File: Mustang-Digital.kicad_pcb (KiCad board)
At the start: 4 copper layers, 67 x 105.4 mm, 125 parts, among them IC307 TPD4E1B06DRLR, IC308 TPD4E1B06DRLR, J1 685119248123_Left, J2 685119248123_Left, J3 Conn_01x02_Pin_JST-PH_Batt, J303 2130830005, J4 Micro_SD_Card_4.0_CUI, U1 BM83SM1-00TB, U2 LP5012RUKR, U3 STM32L496VGTx, U301 SPU03L-05, U302 SPU03L-05, U303 SPU03L-05, U304 ADUM4160BRWZ, U305 USB2422T-I/MJ, U306 BQ24296RGER, U307 TPD4E1B06DRLR, U308 TPD4E1B06DRLR

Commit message: wip
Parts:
- added C12: 1uF, Mustang_Library:C_0805_2012Metric_Pad1.18x1.45mm_HandSolder, F.Cu at (133.5, 113.0)
- added C13: 1uF, Mustang_Library:C_0805_2012Metric_Pad1.18x1.45mm_HandSolder, F.Cu at (136.5, 113.0)
- added U4: LP5907MFX-3.3_NOPB, Mustang_Library:SOT95P280X145-5N, F.Cu at (135.0, 116.8)
- J1, J2: value 685119248123_Left -> 685119248123
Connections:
- net /Buds/IMU_CSR renamed /Buds/HR_INTR
- net /Buds/SPK_AUDIO+L renamed /BT/SPK_AUDIO+L
- net /Buds/SPK_AUDIO+R renamed /BT/SPK_AUDIO+R
- net /Buds/SPK_AUDIO-L renamed /BT/SPK_AUDIO-L
- net /Buds/SPK_AUDIO-R renamed /BT/SPK_AUDIO-R
- net /Buds/TALK_MICL renamed /BT/TALK_MICL
- net /Buds/TALK_MICR renamed /BT/TALK_MICR
- net /Charging_Isolation/5V renamed /Charging_USB/5V
- net /Charging_Isolation/BAT renamed /Charging_USB/BAT
- net /Charging_Isolation/BTST renamed /Charging_USB/BTST
- net /Charging_Isolation/CRFILT renamed /Charging_USB/CRFILT
- net /Charging_Isolation/DM1 renamed /Charging_USB/DM1
- net /Charging_Isolation/DM2 renamed /Charging_USB/DM2
- net /Charging_Isolation/DP1 renamed /Charging_USB/DP1
- net /Charging_Isolation/DP2 renamed /Charging_USB/DP2
- net /Charging_Isolation/ILIM renamed /Charging_USB/ILIM
- net /Charging_Isolation/OCS1_N renamed /Charging_USB/OCS1_N
- net /Charging_Isolation/OCS2_N renamed /Charging_USB/OCS2_N
- net /Charging_Isolation/PLLFILT renamed /Charging_USB/PLLFILT
- net /Charging_Isolation/PMID renamed /Charging_USB/PMID
- net /Charging_Isolation/PRTPWR1 renamed /Charging_USB/PRTPWR1
- net /Charging_Isolation/PRTPWR2 renamed /Charging_USB/PRTPWR2
- net /Charging_Isolation/RBIAS renamed /Charging_USB/RBIAS
- net /Charging_Isolation/REGN renamed /Charging_USB/REGN
- net /Charging_Isolation/RESET_N renamed /Charging_USB/RESET_N
- net /Charging_Isolation/SW renamed /Charging_USB/SW
- net /Charging_Isolation/TS renamed /Charging_USB/TS
- net /Charging_Isolation/VBUS1 renamed /Charging_USB/VBUS1
- net /Charging_Isolation/VBUS_DET renamed /Charging_USB/VBUS_DET
- net /Charging_Isolation/VOUT1 renamed /Charging_USB/VOUT1
- net /Charging_Isolation/VOUT2 renamed /Charging_USB/VOUT2
- net /Charging_Isolation/VOUT3 renamed /Charging_USB/VOUT3
- net /Charging_Isolation/XIN renamed /Charging_USB/XIN
- net /Charging_Isolation/XOUT renamed /Charging_USB/XOUT
- net /LEDS_BUTTONS_SWITCHES/LED_EN renamed /LEDs_Switches/LED_EN
- net /LEDS_BUTTONS_SWITCHES/LED_SCL renamed /LEDs_Switches/LED_SCL
- net /LEDS_BUTTONS_SWITCHES/LED_SDA renamed /LEDs_Switches/LED_SDA
- net /LEDS_BUTTONS_SWITCHES/SW_BTPAIR renamed /LEDs_Switches/SW_BTPAIR
- net /LEDS_BUTTONS_SWITCHES/SW_PLAY renamed /LEDs_Switches/SW_PLAY
- net /LEDS_BUTTONS_SWITCHES/SW_PWR renamed /LEDs_Switches/SW_PWR
- net /LEDS_BUTTONS_SWITCHES/SW_RECORD renamed /LEDs_Switches/SW_RECORD
- C302 pad 2: /Charging_Isolation/VDD1 -> /Charging_USB/VDD1
- C306 pad 1: /Charging_Isolation/VSYS -> /Charging_USB/VSYS
- C307 pad 1: /Charging_Isolation/VSYS -> /Charging_USB/VSYS
- C315 pad 2: /Charging_Isolation/VBUS0 -> /Charging_USB/VBUS0
- C316 pad 2: /Charging_Isolation/VBUS0 -> /Charging_USB/VBUS0
- C7 pad 2: /Buds/VSYS -> /Charging_USB/VSYS
- C8 pad 2: /Buds/VSYS -> /Charging_USB/VSYS
- J1 pad 5: /Buds/VSYS -> /Charging_USB/VSYS
- J2 pad 5: /Buds/VSYS -> /Charging_USB/VSYS
- J303 pad A4: /Charging_Isolation/VBUS0 -> /Charging_USB/VBUS0
- J303 pad A5: /Charging_Isolation/CC1 -> /Charging_USB/CC1
- J303 pad A6: /Charging_Isolation/DA+ -> /Charging_USB/DAB+
- J303 pad A7: /Charging_Isolation/DB- -> /Charging_USB/DAB-
- J303 pad A8: /Charging_Isolation/SBU1 -> /Charging_USB/SBU1
- J303 pad A9: /Charging_Isolation/VBUS0 -> /Charging_USB/VBUS0
- J303 pad B4: /Charging_Isolation/VBUS0 -> /Charging_USB/VBUS0
- J303 pad B5: /Charging_Isolation/CC2 -> /Charging_USB/CC2
- J303 pad B6: /Charging_Isolation/DA+ -> /Charging_USB/DAB+
- J303 pad B7: /Charging_Isolation/DB- -> /Charging_USB/DAB-
- J303 pad B8: /Charging_Isolation/SBU2 -> /Charging_USB/SBU2
- J303 pad B9: /Charging_Isolation/VBUS0 -> /Charging_USB/VBUS0
- L301 pad 2: /Charging_Isolation/VSYS -> /Charging_USB/VSYS
- L305 pad 2: /Charging_Isolation/VBUS0 -> /Charging_USB/VBUS0
- L306 pad 2: /Charging_Isolation/VBUS0 -> /Charging_USB/VBUS0
- R312 pad 2: /Charging_Isolation/PG -> /Charging_USB/PG
- R313 pad 2: /Charging_Isolation/STAT -> /Charging_USB/STAT
- R314 pad 2: /Charging_Isolation/INT -> /Charging_USB/INT
- R315 pad 2: /Charging_Isolation/SCL -> /Charging_USB/SCL
- R316 pad 2: /Charging_Isolation/SDA -> /Charging_USB/SDA
- R317 pad 2: /Charging_Isolation/CC2 -> /Charging_USB/CC2
- R318 pad 2: /Charging_Isolation/CC1 -> /Charging_USB/CC1
- U304 pad 10: /Charging_Isolation/DD+ -> /Charging_USB/DD+
- U304 pad 11: /Charging_Isolation/DD- -> /Charging_USB/DD-
- U304 pad 12: /Charging_Isolation/PIN -> /Charging_USB/PIN
- U304 pad 13: /Charging_Isolation/SPD -> /Charging_USB/SPD
- U304 pad 3: /Charging_Isolation/VDD1 -> /Charging_USB/VDD1
- U304 pad 4: /Charging_Isolation/PDEN -> /Charging_USB/PDEN
- U304 pad 5: /Charging_Isolation/SPU -> /Charging_USB/SPU
- U304 pad 6: /Charging_Isolation/UD- -> /Charging_USB/UD-
- U304 pad 7: /Charging_Isolation/UD+ -> /Charging_USB/UD+
- U305 pad 13: /Charging_Isolation/SMBDATA -> /Charging_USB/SMBDATA
- U305 pad 14: /Charging_Isolation/SMBCLK -> /Charging_USB/SMBCLK
- U305 pad 17: /Charging_Isolation/SUSP_IND -> /Charging_USB/SUSP_IND
- U305 pad 19: /Charging_Isolation/DMU -> /Charging_USB/DMU
- U305 pad 20: /Charging_Isolation/DPU -> /Charging_USB/DPU
- U306 pad 12: /Charging_Isolation/QON -> /Charging_USB/QON
- U306 pad 15: /Charging_Isolation/VSYS -> /Charging_USB/VSYS
- U306 pad 16: /Charging_Isolation/VSYS -> /Charging_USB/VSYS
- U306 pad 2: /Charging_Isolation/PSEL -> /Charging_USB/PSEL
- U306 pad 3: /Charging_Isolation/PG -> /Charging_USB/PG
- U306 pad 4: /Charging_Isolation/STAT -> /Charging_USB/STAT
- U306 pad 5: /Charging_Isolation/SCL -> /Charging_USB/SCL
- U306 pad 6: /Charging_Isolation/SDA -> /Charging_USB/SDA
- U306 pad 7: /Charging_Isolation/INT -> /Charging_USB/INT
- U306 pad 8: /Charging_Isolation/OTG -> /Charging_USB/OTG
- U306 pad 9: /Charging_Isolation/CE -> /Charging_USB/CE
- U307 pad 1: /Charging_Isolation/CC1 -> /Charging_USB/CC1
- U307 pad 3: /Charging_Isolation/VBUS0 -> /Charging_USB/VBUS0
- U307 pad 4: /Charging_Isolation/SBU2 -> /Charging_USB/SBU2
- U307 pad 6: /Charging_Isolation/DA+ -> /Charging_USB/DAB+
- U308 pad 1: /Charging_Isolation/CC2 -> /Charging_USB/CC2
- U308 pad 3: /Charging_Isolation/DB- -> /Charging_USB/DAB-
- U308 pad 4: /Charging_Isolation/SBU1 -> /Charging_USB/SBU1
- U308 pad 6: /Charging_Isolation/VBUS0 -> /Charging_USB/VBUS0
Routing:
- net /Charging_USB/VBUS0: track 0.00 -> 12.6 mm
- net /Charging_Isolation/VBUS0: track 12.6 -> 0.00 mm
- net /Charging_USB/VSYS: track 0.00 -> 7.13 mm
- net /Buds/VSYS: track 7.13 -> 0.00 mm
- net /Charging_USB/CC2: track 0.00 -> 5.84 mm
- net /Charging_Isolation/CC2: track 5.84 -> 0.00 mm
- net /Charging_USB/CC1: track 0.00 -> 5.04 mm
- net /Charging_Isolation/CC1: track 5.04 -> 0.00 mm
- net /Charging_USB/SBU2: track 0.00 -> 3.27 mm
- net /Charging_Isolation/SBU2: track 3.27 -> 0.00 mm
- net /Charging_USB/SBU1: track 0.00 -> 3.07 mm
- net /Charging_Isolation/SBU1: track 3.07 -> 0.00 mm
- net /Charging_USB/QON: vias 0 -> 1
- net /Charging_Isolation/QON: vias 1 -> 0

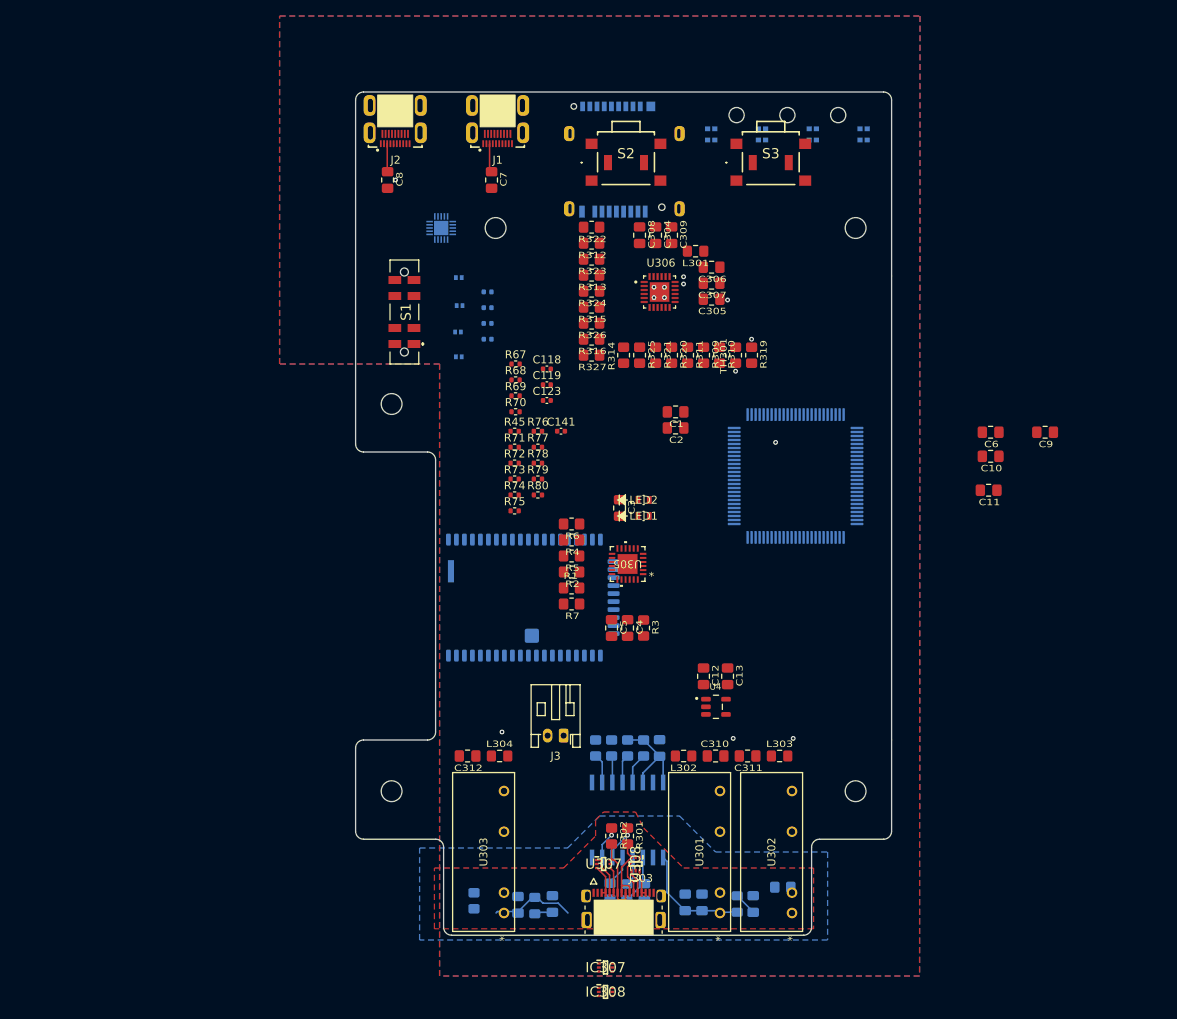
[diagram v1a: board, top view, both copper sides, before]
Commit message: Use all YAGEO 0603 resistors.
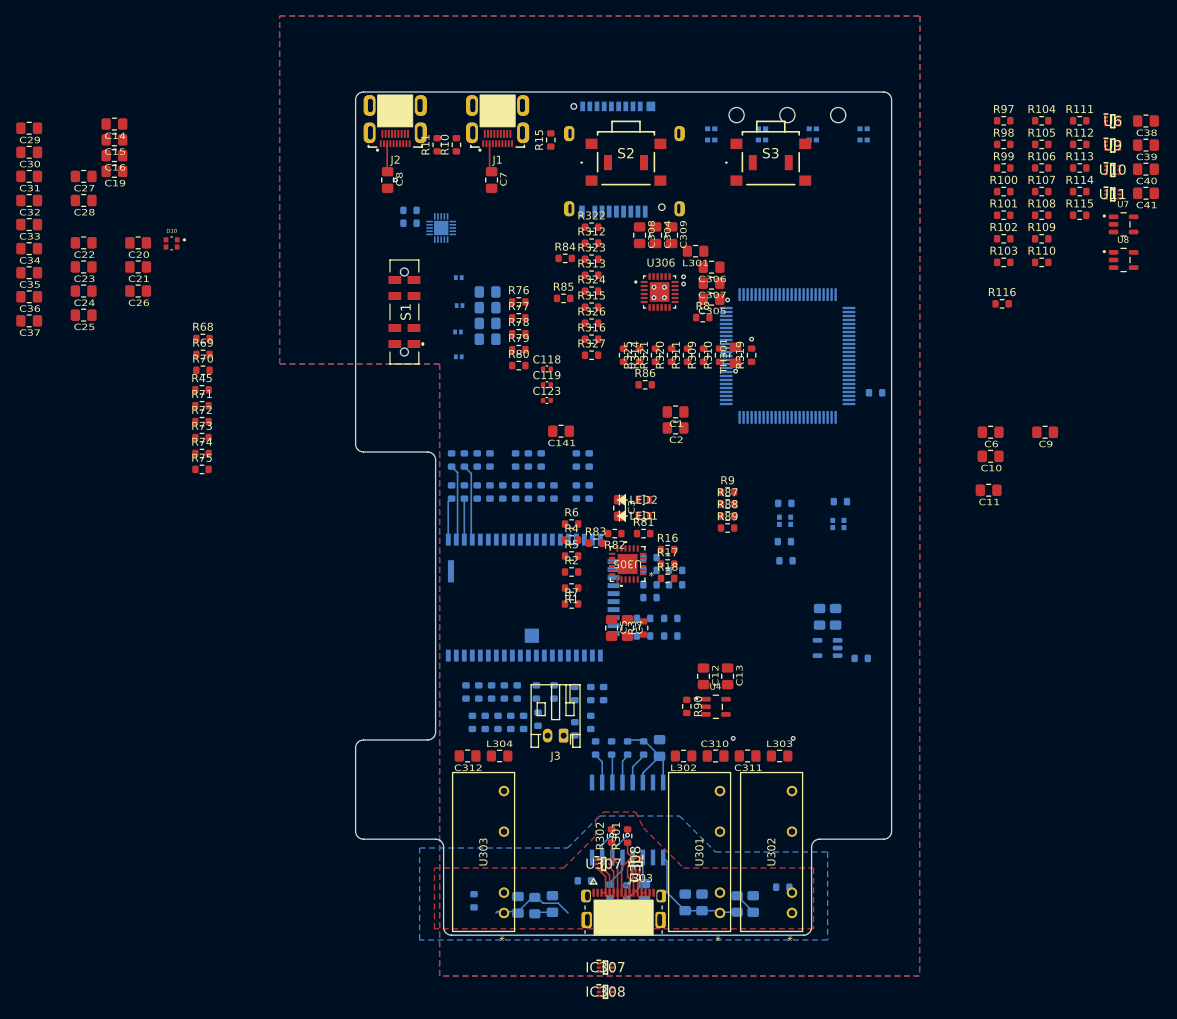
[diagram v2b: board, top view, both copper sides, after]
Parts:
- removed ?: , 
- removed MH1: Mounting_Holes, Mustang_Library:Mounting_Holes
- added C14: .1uF, Mustang_Library:C_0805_2012Metric_Pad1.18x1.45mm_HandSolder, F.Cu at (59.9, 44.0)
- added C15: 10nF, Mustang_Library:C_0805_2012Metric_Pad1.18x1.45mm_HandSolder, F.Cu at (59.9, 46.0)
- added C16: 10nF, Mustang_Library:C_0805_2012Metric_Pad1.18x1.45mm_HandSolder, F.Cu at (59.9, 48.0)
- added C17: 1uF, Mustang_Library:C_0805_2012Metric_Pad1.18x1.45mm_HandSolder, B.Cu at (150.0, 105.6)
- added C18: 1uF, Mustang_Library:C_0805_2012Metric_Pad1.18x1.45mm_HandSolder, B.Cu at (148.0, 105.6)
- added C19: .1uF, Mustang_Library:C_0805_2012Metric_Pad1.18x1.45mm_HandSolder, F.Cu at (59.9, 49.9)
- added C20: 0.1uF, Mustang_Library:C_0805_2012Metric_Pad1.18x1.45mm_HandSolder, F.Cu at (62.8, 58.9)
- added C21: 0.1uF, Mustang_Library:C_0805_2012Metric_Pad1.18x1.45mm_HandSolder, F.Cu at (62.8, 61.9)
- added C22: 0.1uF, Mustang_Library:C_0805_2012Metric_Pad1.18x1.45mm_HandSolder, F.Cu at (56.0, 58.9)
- added C23: 0.1uF, Mustang_Library:C_0805_2012Metric_Pad1.18x1.45mm_HandSolder, F.Cu at (56.0, 61.9)
- added C24: 0.1uF, Mustang_Library:C_0805_2012Metric_Pad1.18x1.45mm_HandSolder, F.Cu at (56.0, 64.9)
- added C25: 0.1uF, Mustang_Library:C_0805_2012Metric_Pad1.18x1.45mm_HandSolder, F.Cu at (56.0, 67.9)
- added C26: 0.1uF, Mustang_Library:C_0805_2012Metric_Pad1.18x1.45mm_HandSolder, F.Cu at (62.8, 64.9)
- added C27: 0.1uF, Mustang_Library:C_0805_2012Metric_Pad1.18x1.45mm_HandSolder, F.Cu at (56.0, 50.5)
- added C28: 0.1uF, Mustang_Library:C_0805_2012Metric_Pad1.18x1.45mm_HandSolder, F.Cu at (56.0, 53.6)
- added C29: 0.1uF, Mustang_Library:C_0805_2012Metric_Pad1.18x1.45mm_HandSolder, F.Cu at (49.2, 44.5)
- added C30: 0.1uF, Mustang_Library:C_0805_2012Metric_Pad1.18x1.45mm_HandSolder, F.Cu at (49.2, 47.5)
- added C31: 0.1uF, Mustang_Library:C_0805_2012Metric_Pad1.18x1.45mm_HandSolder, F.Cu at (49.2, 50.5)
- added C32: 0.1uF, Mustang_Library:C_0805_2012Metric_Pad1.18x1.45mm_HandSolder, F.Cu at (49.2, 53.6)
- added C33: 0.1uF, Mustang_Library:C_0805_2012Metric_Pad1.18x1.45mm_HandSolder, F.Cu at (49.2, 56.6)
- added C34: 0.1uF, Mustang_Library:C_0805_2012Metric_Pad1.18x1.45mm_HandSolder, F.Cu at (49.2, 59.6)
- added C35: 0.1uF, Mustang_Library:C_0805_2012Metric_Pad1.18x1.45mm_HandSolder, F.Cu at (49.2, 62.6)
- added C36: 0.1uF, Mustang_Library:C_0805_2012Metric_Pad1.18x1.45mm_HandSolder, F.Cu at (49.2, 65.6)
- added C37: 1uF, Mustang_Library:C_0805_2012Metric_Pad1.18x1.45mm_HandSolder, F.Cu at (49.2, 68.6)
- added C38: 1uF, Mustang_Library:C_0805_2012Metric_Pad1.18x1.45mm_HandSolder, F.Cu at (188.8, 43.6)
- added C39: 1uF, Mustang_Library:C_0805_2012Metric_Pad1.18x1.45mm_HandSolder, F.Cu at (188.8, 46.6)
- added C40: 1uF, Mustang_Library:C_0805_2012Metric_Pad1.18x1.45mm_HandSolder, F.Cu at (188.8, 49.6)
- added C41: 1uF, Mustang_Library:C_0805_2012Metric_Pad1.18x1.45mm_HandSolder, F.Cu at (188.8, 52.7)
- added D10: EAST1616RGBA3, Mustang_Library:LED_EAST1616RGBA3, F.Cu at (67.0, 58.9)
- added D11: EAST1616RGBA3, Mustang_Library:LED_EAST1616RGBA3, B.Cu at (143.7, 93.6)
- added D9: EAST1616RGBA3, Mustang_Library:LED_EAST1616RGBA3, B.Cu at (150.3, 94.0)
- added R10: 0R, Mustang_Library:R_0603_1608Metric, F.Cu at (102.6, 46.6)
- added R100: 24R, Mustang_Library:R_0603_1608Metric, F.Cu at (171.0, 52.5)
- added R101: 24R, Mustang_Library:R_0603_1608Metric, F.Cu at (171.0, 55.4)
- added R102: 24R, Mustang_Library:R_0603_1608Metric, F.Cu at (171.0, 58.4)
- added R103: 24R, Mustang_Library:R_0603_1608Metric, F.Cu at (171.0, 61.3)
- added R104: 24R, Mustang_Library:R_0603_1608Metric, F.Cu at (175.8, 43.6)
- added R105: 24R, Mustang_Library:R_0603_1608Metric, F.Cu at (175.8, 46.5)
- added R106: 24R, Mustang_Library:R_0603_1608Metric, F.Cu at (175.8, 49.5)
- added R107: 24R, Mustang_Library:R_0603_1608Metric, F.Cu at (175.8, 52.5)
- added R108: 24R, Mustang_Library:R_0603_1608Metric, F.Cu at (175.8, 55.4)
- added R109: 24R, Mustang_Library:R_0603_1608Metric, F.Cu at (175.8, 58.4)
- added R11: 0R, Mustang_Library:R_0603_1608Metric, F.Cu at (100.2, 46.6)
- added R110: 24R, Mustang_Library:R_0603_1608Metric, F.Cu at (175.8, 61.3)
- added R111: 24R, Mustang_Library:R_0603_1608Metric, F.Cu at (180.5, 43.6)
- added R112: 24R, Mustang_Library:R_0603_1608Metric, F.Cu at (180.5, 46.5)
- added R113: 24R, Mustang_Library:R_0603_1608Metric, F.Cu at (180.5, 49.5)
- added R114: 24R, Mustang_Library:R_0603_1608Metric, F.Cu at (180.5, 52.5)
- added R115: 24R, Mustang_Library:R_0603_1608Metric, F.Cu at (180.5, 55.4)
- added R116: 0R, Mustang_Library:R_0603_1608Metric, F.Cu at (170.8, 66.5)
- added R12: 0R, Mustang_Library:R_0603_1608Metric, B.Cu at (118.6, 138.6)
- added R13: 0R, Mustang_Library:R_0603_1608Metric, B.Cu at (96.8, 56.4)
- added R14: 0R, Mustang_Library:R_0603_1608Metric, B.Cu at (96.8, 54.8)
- added R15: 0R, Mustang_Library:R_0603_1608Metric, F.Cu at (114.4, 46.0)
- added R16: 24R, Mustang_Library:R_0603_1608Metric, F.Cu at (129.0, 97.2)
- added R17: 24R, Mustang_Library:R_0603_1608Metric, F.Cu at (129.0, 99.0)
- added R18: 24R, Mustang_Library:R_0603_1608Metric, F.Cu at (129.0, 100.8)
- added R19: 24R, Mustang_Library:R_0603_1608Metric, B.Cu at (114.8, 115.0)
- added R20: 24R, Mustang_Library:R_0603_1608Metric, B.Cu at (126.0, 108.0)
- added R21: 24R, Mustang_Library:R_0603_1608Metric, B.Cu at (129.4, 108.0)
- added R22: 24R, Mustang_Library:R_0603_1608Metric, B.Cu at (121.0, 115.2)
- added R23: 24R, Mustang_Library:R_0603_1608Metric, B.Cu at (104.6, 118.8)
- added R24: 24R, Mustang_Library:R_0603_1608Metric, B.Cu at (103.8, 115.0)
- added R25: 24R, Mustang_Library:R_0603_1608Metric, B.Cu at (105.4, 115.0)
- added R26: 24R, Mustang_Library:R_0603_1608Metric, B.Cu at (106.2, 118.8)
- added R27: 24R, Mustang_Library:R_0603_1608Metric, B.Cu at (107.8, 118.8)
- added R28: 24R, Mustang_Library:R_0603_1608Metric, B.Cu at (119.4, 118.8)
- added R29: 24R, Mustang_Library:R_0603_1608Metric, B.Cu at (112.8, 118.4)
- added R30: 24R, Mustang_Library:R_0603_1608Metric, B.Cu at (111.0, 118.8)
- added R31: 24R, Mustang_Library:R_0603_1608Metric, B.Cu at (117.4, 119.6)
- added R32: 24R, Mustang_Library:R_0603_1608Metric, B.Cu at (107.0, 115.0)
- added R33: 24R, Mustang_Library:R_0603_1608Metric, B.Cu at (109.4, 118.8)
- added R34: 24R, Mustang_Library:R_0603_1608Metric, B.Cu at (110.2, 115.0)
- added R35: 24R, Mustang_Library:R_0603_1608Metric, B.Cu at (126.8, 98.2)
- added R36: 24R, Mustang_Library:R_0603_1608Metric, B.Cu at (112.6, 115.0)
- added R37: 24R, Mustang_Library:R_0603_1608Metric, B.Cu at (119.2, 86.0)
- added R38: 24R, Mustang_Library:R_0603_1608Metric, B.Cu at (102.0, 90.0)
- added R39: 24R, Mustang_Library:R_0603_1608Metric, B.Cu at (102.0, 86.0)
- added R40: 24R, Mustang_Library:R_0603_1608Metric, B.Cu at (103.6, 90.0)
- added R41: 24R, Mustang_Library:R_0603_1608Metric, B.Cu at (103.6, 86.0)
- added R42: 24R, Mustang_Library:R_0603_1608Metric, B.Cu at (105.2, 90.0)
- added R43: 0R, Mustang_Library:R_0603_1608Metric, B.Cu at (105.2, 86.0)
- added R44: 0R, Mustang_Library:R_0603_1608Metric, B.Cu at (106.8, 86.0)
- added R46: 0R, Mustang_Library:R_0603_1608Metric, B.Cu at (108.4, 90.0)
- added R47: 24R, Mustang_Library:R_0603_1608Metric, B.Cu at (111.6, 90.0)
- added R48: 24R, Mustang_Library:R_0603_1608Metric, B.Cu at (111.6, 86.0)
- added R49: 0R, Mustang_Library:R_0603_1608Metric, B.Cu at (110.0, 90.0)
- added R50: 0R, Mustang_Library:R_0603_1608Metric, B.Cu at (110.0, 86.0)
- added R51: 0R, Mustang_Library:R_0603_1608Metric, B.Cu at (113.2, 90.0)
- added R52: 0R, Mustang_Library:R_0603_1608Metric, B.Cu at (113.2, 86.0)
- added R53: 0R, Mustang_Library:R_0603_1608Metric, B.Cu at (114.8, 90.0)
- added R54: 24R, Mustang_Library:R_0603_1608Metric, B.Cu at (117.6, 90.0)
- added R55: 24R, Mustang_Library:R_0603_1608Metric, B.Cu at (117.6, 86.0)
- added R56: 24R, Mustang_Library:R_0603_1608Metric, B.Cu at (119.2, 90.0)
- added R57: 0R, Mustang_Library:R_0603_1608Metric, B.Cu at (126.8, 99.8)
- added R58: 0R, Mustang_Library:R_0603_1608Metric, B.Cu at (130.0, 99.8)
- added R59: 0R, Mustang_Library:R_0603_1608Metric, B.Cu at (126.8, 101.6)
- added R60: 24R, Mustang_Library:R_0603_1608Metric, B.Cu at (130.0, 101.6)
- added R61: 24R, Mustang_Library:R_0603_1608Metric, B.Cu at (126.8, 103.2)
- added R62: 24R, Mustang_Library:R_0603_1608Metric, B.Cu at (108.6, 115.0)
- added R63: 0R, Mustang_Library:R_0603_1608Metric, B.Cu at (119.4, 115.2)
- added R64: 0R, Mustang_Library:R_0603_1608Metric, B.Cu at (117.4, 115.2)
- added R65: 0R, Mustang_Library:R_0603_1608Metric, B.Cu at (129.4, 105.8)
- added R66: 0R, Mustang_Library:R_0603_1608Metric, B.Cu at (126.0, 105.8)
- added R8: 0R, Mustang_Library:R_0603_1608Metric, F.Cu at (133.4, 68.2)
- added R81: 24R, Mustang_Library:R_0603_1608Metric, F.Cu at (126.0, 95.2)
- added R82: 24R, Mustang_Library:R_0603_1608Metric, F.Cu at (122.4, 95.2)
- added R83: 24R, Mustang_Library:R_0603_1608Metric, F.Cu at (120.0, 96.4)
- added R84: 5.23K, Mustang_Library:R_0603_1608Metric, F.Cu at (116.2, 60.8)
- added R85: 5.23K, Mustang_Library:R_0603_1608Metric, F.Cu at (116.0, 65.8)
- added R86: 5.23K, Mustang_Library:R_0603_1608Metric, F.Cu at (126.2, 76.6)
- added R87: 0R, Mustang_Library:R_0603_1608Metric, F.Cu at (136.5, 91.5)
- added R88: 0R, Mustang_Library:R_0603_1608Metric, F.Cu at (136.5, 93.0)
- added R89: 0R, Mustang_Library:R_0603_1608Metric, F.Cu at (136.5, 94.5)
- added R9: 0R, Mustang_Library:R_0603_1608Metric, F.Cu at (136.5, 90.0)
- added R90: 24R, Mustang_Library:R_0603_1608Metric, F.Cu at (131.4, 116.8)
- added R91: 5.23K, Mustang_Library:R_0603_1608Metric, B.Cu at (143.8, 98.6)
- added R92: 5.23K, Mustang_Library:R_0603_1608Metric, B.Cu at (143.6, 96.2)
- added R93: 5.23K, Mustang_Library:R_0603_1608Metric, B.Cu at (143.6, 91.4)
- added R94: 10K, Mustang_Library:R_0603_1608Metric, B.Cu at (150.6, 91.2)
- added R95: 0R, Mustang_Library:R_0603_1608Metric, B.Cu at (155.0, 77.6)
- added R96: 24R, Mustang_Library:R_0603_1608Metric, B.Cu at (153.2, 110.8)
- added R97: 24R, Mustang_Library:R_0603_1608Metric, F.Cu at (171.0, 43.6)
- added R98: 24R, Mustang_Library:R_0603_1608Metric, F.Cu at (171.0, 46.5)
- added R99: 24R, Mustang_Library:R_0603_1608Metric, F.Cu at (171.0, 49.5)
- added U10: TPD4E1B06DRLR, Mustang_Library:SOTFL50P160X60-6N, F.Cu at (184.6, 49.8)
- added U11: TPD4E1B06DRLR, Mustang_Library:SOTFL50P160X60-6N, F.Cu at (184.6, 52.8)
- added U5: LP5907MFX-3.3_NOPB, Mustang_Library:SOT95P280X145-5N, B.Cu at (149.0, 109.5)
- added U6: TPD4E1B06DRLR, Mustang_Library:SOTFL50P160X60-6N, F.Cu at (184.6, 43.6)
- added U7: LP5907MFX-3.3_NOPB, Mustang_Library:SOT95P280X145-5N, F.Cu at (186.0, 56.5)
- added U8: LP5907MFX-1.8_NOPB, Mustang_Library:SOT95P280X145-5N, F.Cu at (186.0, 61.0)
- added U9: TPD4E1B06DRLR, Mustang_Library:SOTFL50P160X60-6N, F.Cu at (184.6, 46.7)
- C141, C142, C143, C144, C145: footprint Mustang_Library:C_0402_1005Metric -> Mustang_Library:C_0805_2012Metric_Pad1.18x1.45mm_HandSolder
- R1, R2: value 100k -> 100K; footprint Mustang_Library:R_0805_2012Metric_Pad1.20x1.40mm_HandSolder -> Mustang_Library:R_0603_1608Metric
- R3: value 12k -> 12K; footprint Mustang_Library:R_0805_2012Metric_Pad1.20x1.40mm_HandSolder -> Mustang_Library:R_0603_1608Metric
- R301, R302, R303, R304, R319, R320, R321, R322, R323, R324, R325, R326, R327, R4, R5, R6, R7: footprint Mustang_Library:R_0805_2012Metric_Pad1.20x1.40mm_HandSolder -> Mustang_Library:R_0603_1608Metric
- R305, R306, R307, R308: value 24R -> 10K; footprint Mustang_Library:R_0805_2012Metric_Pad1.20x1.40mm_HandSolder -> Mustang_Library:R_0603_1608Metric
- R309: value 31.23k -> 30.9K; footprint Mustang_Library:R_0805_2012Metric_Pad1.20x1.40mm_HandSolder -> Mustang_Library:R_0603_1608Metric
- R310: value 5.25k -> 5.23K; footprint Mustang_Library:R_0805_2012Metric_Pad1.20x1.40mm_HandSolder -> Mustang_Library:R_0603_1608Metric
- R311: value 250R -> 249R; footprint Mustang_Library:R_0805_2012Metric_Pad1.20x1.40mm_HandSolder -> Mustang_Library:R_0603_1608Metric
- R312, R313, R314, R315, R316: value 10k -> 10K; footprint Mustang_Library:R_0805_2012Metric_Pad1.20x1.40mm_HandSolder -> Mustang_Library:R_0603_1608Metric
- R317, R318: value 5.1k -> 5.23K; footprint Mustang_Library:R_0805_2012Metric_Pad1.20x1.40mm_HandSolder -> Mustang_Library:R_0603_1608Metric
- R45, R72, R77, R79: value 1k -> 1K; footprint Mustang_Library:R_0402_1005Metric -> Mustang_Library:R_0603_1608Metric
- R67: value 33R -> 0R; footprint Mustang_Library:R_0402_1005Metric -> Mustang_Library:R_0603_1608Metric; moved to B.Cu
- R68, R69: value 33R -> 0R; footprint Mustang_Library:R_0402_1005Metric -> Mustang_Library:R_0603_1608Metric
- R70: value 33R -> 24R; footprint Mustang_Library:R_0402_1005Metric -> Mustang_Library:R_0603_1608Metric
- R71, R73, R74, R75, R78, R80: value 10k -> 10K; footprint Mustang_Library:R_0402_1005Metric -> Mustang_Library:R_0603_1608Metric
- R76: value 2.7k -> 2.7K; footprint Mustang_Library:R_0402_1005Metric -> Mustang_Library:R_0603_1608Metric
- U1: footprint Mustang_Library:Microchip_BM83 -> Mustang_Library:BM83_MCH
- U3: value STM32L496VGTx -> STM32L496VGT6_Mustang; footprint Mustang_Library:LQFP-100_14x14mm_P0.5mm -> Package_QFP:LQFP-100_14x14mm_P0.5mm
- moved R45 39.4 mm to (70.8, 77.2)
- moved R68 39.4 mm to (70.9, 70.8)
- moved R69 39.4 mm to (70.9, 72.8)
- moved R70 39.4 mm to (70.9, 74.8)
- moved R71 39.4 mm to (70.8, 79.2)
- moved R72 39.4 mm to (70.8, 81.2)
- moved R73 39.4 mm to (70.8, 83.2)
- moved R74 39.4 mm to (70.8, 85.2)
- moved R75 39.4 mm to (70.8, 87.2)
- moved R76 16.3 mm to (110.4, 66.2)
- moved R77 16.3 mm to (110.4, 68.2)
- moved R78 16.3 mm to (110.4, 70.2)
- moved R79 16.3 mm to (110.4, 72.2)
- moved R80 16.3 mm to (110.4, 74.2)
- moved R67 16.3 mm to (106.8, 90.0), turned to -90 degrees
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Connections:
- net +BATT renamed Net-(J3-+Batt)
- net -BATT renamed Net-(J3--Batt)
- net /Charging_Isolation/BQCE renamed /Charging_USB/BAT_CE
- net /Charging_Isolation/BQOTG renamed /Charging_USB/BAT_OTG
- net /Charging_Isolation/BQPSEL renamed /Charging_USB/BAT_PSEL
- net /Charging_Isolation/BQQON renamed /Charging_USB/BAT_QON
- net /Charging_Isolation/SCL renamed /Charging_USB/BAT_SCL
- net /Charging_Isolation/SDA renamed /Charging_USB/BAT_SDA
- net /Charging_Isolation/USBRESET_N renamed /Charging_USB/USB_SMBDATA
- net /Charging_Isolation/USBSMBCLK renamed /Charging_USB/USB_SMBCLK
- C303 pad 2: +3V3 -> Net-(U304-VDD2)
- J1 pad 1: /BT/SPK_AUDIO+L -> /SPK_AUDIO+L
- J1 pad 2: /BT/SPK_AUDIO-L -> /SPK_AUDIO-L
- J1 pad 6: /BT/TALK_MICL -> /TALK_MICL
- J2 pad 1: /BT/SPK_AUDIO+R -> /SPK_AUDIO+R
- J2 pad 2: /BT/SPK_AUDIO-R -> /SPK_AUDIO-R
- J2 pad 6: /BT/TALK_MICR -> /TALK_MICR
- J4 pad 1: unconnected-(J4-DAT2-Pad1) -> Net-(J4-DAT2)
- J4 pad 15: unconnected-(J4-VDD_1.8-Pad15) -> Net-(J4-VDD_1.8)
- J4 pad 16: unconnected-(J4-SWIO-Pad16) -> Net-(J4-SWIO)
- J4 pad 17: unconnected-(J4-VSS-Pad17) -> GND
- J4 pad 18: unconnected-(J4-D0+-Pad18) -> Net-(J4-D0+)
- J4 pad 19: unconnected-(J4-D0--Pad19) -> Net-(J4-D0-)
- J4 pad 2: unconnected-(J4-DAT3/CD-Pad2) -> Net-(J4-DAT3/CD)
- J4 pad 20: unconnected-(J4-VSS-Pad20) -> GND
- J4 pad 21: unconnected-(J4-D1--Pad21) -> GND
- J4 pad 22: unconnected-(J4-D1+-Pad22) -> Net-(J4-D1+)
- J4 pad 23: unconnected-(J4-VSS-Pad23) -> GND
- J4 pad 3: unconnected-(J4-CMD-Pad3) -> Net-(J4-CMD)
- J4 pad 4: unconnected-(J4-VDD_3.3-Pad4) -> Net-(J4-VDD_3.3)
- J4 pad 5: unconnected-(J4-CLK-Pad5) -> Net-(J4-CLK)
- J4 pad 6: unconnected-(J4-VSS-Pad6) -> GND
- J4 pad 7: unconnected-(J4-DAT0/RCLK+-Pad7) -> Net-(J4-DAT0/RCLK+)
- J4 pad 8: unconnected-(J4-DAT1/RCLK--Pad8) -> Net-(J4-DAT1/RCLK-)
- J4 pad 9: unconnected-(J4-CD-Pad9) -> Net-(J4-CD)
- R1 pad 1: /Charging_USB/VBUS_DET -> GND
- R1 pad 2: GND -> /Charging_USB/VBUS_DET
- R3 pad 1: GND -> /Charging_USB/RBIAS
- R3 pad 2: /Charging_USB/RBIAS -> GND
- R301 pad 1: /Charging_Isolation/DB- -> /Charging_USB/DAB-
- R301 pad 2: /Charging_Isolation/UD- -> /Charging_USB/UD-
- R302 pad 1: /Charging_Isolation/DA+ -> /Charging_USB/DAB+
- R302 pad 2: /Charging_Isolation/UD+ -> /Charging_USB/UD+
- R303 pad 1: /Charging_Isolation/DD- -> /Charging_USB/DD-
- R303 pad 2: /Charging_Isolation/DMU -> /Charging_USB/DMU
- R304 pad 1: /Charging_Isolation/DD+ -> /Charging_USB/DD+
- R304 pad 2: /Charging_Isolation/DPU -> /Charging_USB/DPU
- R305 pad 1: /Charging_Isolation/VDD1 -> /Charging_USB/VDD1
- R305 pad 2: /Charging_Isolation/SPU -> /Charging_USB/SPU
- R306 pad 1: /Charging_Isolation/VDD1 -> /Charging_USB/VDD1
- R306 pad 2: /Charging_Isolation/PDEN -> /Charging_USB/PDEN
- R307 pad 1: /Charging_Isolation/SPD -> /Charging_USB/SPD
- R307 pad 2: /Charging_Isolation/3V3 -> Net-(U304-VDD2)
- R308 pad 1: /Charging_Isolation/PIN -> /Charging_USB/PIN
- R308 pad 2: /Charging_Isolation/3V3 -> Net-(U304-VDD2)
- R312 pad 1: +3V3 -> unconnected-(R312-Pad1)
- R312 pad 2: /Charging_USB/PG -> unconnected-(R312-Pad2)
- R313 pad 1: +3V3 -> unconnected-(R313-Pad1)
- R313 pad 2: /Charging_USB/STAT -> unconnected-(R313-Pad2)
- R314 pad 1: +3V3 -> unconnected-(R314-Pad1)
- R314 pad 2: /Charging_USB/INT -> unconnected-(R314-Pad2)
- R315 pad 1: +3V3 -> unconnected-(R315-Pad1)
- R315 pad 2: /Charging_USB/SCL -> unconnected-(R315-Pad2)
- R316 pad 1: +3V3 -> unconnected-(R316-Pad1)
- R316 pad 2: /Charging_USB/SDA -> unconnected-(R316-Pad2)
- R318 pad 1: GNDPWR -> /Charging_USB/CC1
- R318 pad 2: /Charging_USB/CC1 -> GNDPWR
- R319 pad 2: /Charging_Isolation/QON -> /Charging_USB/QON
- R320 pad 2: /Charging_Isolation/CE -> /Charging_USB/CE
- R321 pad 2: /Charging_Isolation/OTG -> /Charging_USB/OTG
- R322 pad 2: /Charging_Isolation/PSEL -> /Charging_USB/PSEL
- R323 pad 1: /Charging_Isolation/BQPG -> /Charging_USB/BAT_PG
- R323 pad 2: /Charging_Isolation/PG -> /Charging_USB/PG
- R324 pad 1: /Charging_Isolation/BQSTAT -> /Charging_USB/BAT_STAT
- R324 pad 2: /Charging_Isolation/STAT -> /Charging_USB/STAT
- R325 pad 1: /Charging_Isolation/BQINT -> /Charging_USB/BAT_INT
- R325 pad 2: /Charging_Isolation/INT -> /Charging_USB/INT
- R326 pad 2: /Charging_Isolation/_SCL -> /Charging_USB/SCL
- R327 pad 2: /Charging_Isolation/_SDA -> /Charging_USB/SDA
- R4 pad 2: /Charging_Isolation/SMBCLK -> /Charging_USB/SMBCLK
- R5 pad 2: /Charging_Isolation/_RESET_N -> /Charging_USB/SMBDATA
- R6 pad 1: /Charging_Isolation/USBSMBDATA -> /Charging_USB/USB_RESET_N
- R6 pad 2: /Charging_Isolation/SMBDATA -> /Charging_USB/RESET_N
- R67 pad 1: USART1Rx -> /SPK_AUDIO-L
- R67 pad 2: Net-(U1-P8_5/UART_TXD) -> Net-(U1-AOHPM)
- R68 pad 1: USART1Tx -> /Charging_USB/BAT
- R68 pad 2: Net-(U1-P8_6/UART_RXD) -> Net-(U5-OUT)
- R69 pad 1: USART1CTS -> +3V3
- R69 pad 2: Net-(U1-P3_4/UART_RTS) -> Net-(U5-OUT)
- R7 pad 1: /Charging_Isolation/USBSUSP_IND -> /Charging_USB/USB_SUSP_IND
- R7 pad 2: /Charging_Isolation/SUSP_IND -> /Charging_USB/SUSP_IND
- R70 pad 1: USART1RTS -> /Charging_USB/PRTPWR1
- R70 pad 2: Net-(U1-P3_7/UART_CTS) -> unconnected-(R70-Pad2)
- R76 pad 1: Net-(U2-IREF) -> GND
- R76 pad 2: GND -> Net-(U2-IREF)
- R79 pad 1: /LEDs_Switches/SW_BTPAIR -> Net-(S1-NO_3)
- R79 pad 2: Net-(S1-NO_3) -> /LEDs_Switches/SW_BTPAIR
- U1 pad 1: i2SMDR1 -> Net-(U1-DR1)
- U1 pad 10: RIGHT_TM_OUT -> Net-(U1-MICP2)
- U1 pad 11: AIR -> Net-(U1-AIR)
- U1 pad 12: AIL -> Net-(U1-AIL)
- U1 pad 13: unconnected-(U1-MICN1-Pad13) -> Net-(U1-MICN1)
- U1 pad 14: LEFT_TM_OUT -> Net-(U1-MICP1)
- U1 pad 15: unconnected-(U1-MICBIAS-Pad15) -> Net-(U1-MICBIAS)
- U1 pad 17: unconnected-(U1-DMIC_CLK-Pad17) -> Net-(U1-DMIC_CLK)
- U1 pad 18: unconnected-(U1-MDIC1_R-Pad18) -> Net-(U1-DMIC1_R)
- U1 pad 19: unconnected-(U1-MDIC1_L-Pad19) -> Net-(U1-DMIC1_L)
- U1 pad 2: i2SMRFS1 -> Net-(U1-RFS1)
- U1 pad 20: P3_2 -> Net-(U1-P3_2)
- U1 pad 21: P2_6 -> Net-(U1-P2_6)
- U1 pad 22: unconnected-(U1-ADAP_IN-Pad22) -> Net-(U1-ADAP_IN)
- U1 pad 23: unconnected-(U1-BAT_IN-Pad23) -> Net-(U1-BAT_IN)
- U1 pad 24: /BT/SYS_PWR -> Net-(U1-SYS_PWR)
- U1 pad 25: unconnected-(U1-VDD_IO-Pad25) -> Net-(U1-VDD_IO)
- U1 pad 26: P_EN -> Net-(U1-PWR(MFB))
- U1 pad 27: unconnected-(U1-SKI_AMB_DET-Pad27) -> Net-(U1-SKI_AMB_DET)
- U1 pad 28: unconnected-(U1-SK2_KEY_AD-Pad28) -> Net-(U1-SK2_KEY_AD)
- U1 pad 3: i2SMCK -> Net-(U1-SCLK1)
- U1 pad 33: P0_2 -> Net-(U1-P0_2)
- U1 pad 35: P0_6 -> Net-(U1-P0_6)
- U1 pad 36: BTDM -> /BT/USB_DM
- U1 pad 37: BTDP -> /BT/USB_DP
- U1 pad 38: P0_3 -> Net-(U1-P0_3)
- U1 pad 39: P2_7 -> Net-(U1-P2_7)
- U1 pad 4: i2SMDT1 -> Net-(U1-DT1)
- U1 pad 40: P0_5 -> Net-(U1-P0_5)
- U1 pad 41: PWM1 -> Net-(U1-P1_6/PWM1)
- U1 pad 42: P2_3 -> Net-(U1-P2_3)
- U1 pad 43: RST_N -> Net-(U1-RST_N)
- U1 pad 44: P0_0 -> Net-(U1-P0_1)
- U1 pad 45: P0_7 -> Net-(U1-P0_7)
- U1 pad 46: TDI_CPU -> Net-(U1-P1_2/TDI_CPU/SCL)
- U1 pad 47: TCK_CPU -> Net-(U1-P1_3/TCK_CPU/SDA)
- U1 pad 49: Wakeup -> Net-(U1-P0_0/UART_TX_IND)
- U1 pad 5: i2SMCK -> Net-(U1-MCLK1)
- U1 pad 6: /BT/SPKR+ -> Net-(U1-AOHPR)
- U1 pad 7: /BT/SPK- -> Net-(U1-AOHPM)
- U1 pad 8: /BT/SPKL+ -> Net-(U1-AOHPL)
- U1 pad 9: unconnected-(U1-MICN2-Pad9) -> Net-(U1-MICN2)
- U3 pad 100: unconnected-(U3-VDD-Pad100) -> +3V3
- U3 pad 11: unconnected-(U3-VDD-Pad11) -> +3V3
- U3 pad 17: unconnected-(U3-PC2-Pad17) -> Net-(U3-PC2)
- U3 pad 18: unconnected-(U3-PC3-Pad18) -> Net-(U3-PC3)
- U3 pad 22: unconnected-(U3-VDDA-Pad22) -> Net-(U3-VDDA)
- U3 pad 28: unconnected-(U3-VDD-Pad28) -> +3V3
- U3 pad 33: unconnected-(U3-PC4-Pad33) -> Net-(U3-PC4)
- U3 pad 34: unconnected-(U3-PC5-Pad34) -> Net-(U3-PC5)
- U3 pad 50: unconnected-(U3-VDD-Pad50) -> +3V3
- U3 pad 6: unconnected-(U3-VBAT-Pad6) -> /MCU/VBAT
- U3 pad 63: unconnected-(U3-PC6-Pad63) -> Net-(U3-PC6)
- U3 pad 64: unconnected-(U3-PC7-Pad64) -> Net-(U3-PC7)
- U3 pad 65: unconnected-(U3-PC8-Pad65) -> Net-(U3-PC8)
- U3 pad 66: unconnected-(U3-PC9-Pad66) -> Net-(U3-PC9)
- U3 pad 67: unconnected-(U3-PA8-Pad67) -> Net-(U3-PA8)
- U3 pad 68: unconnected-(U3-PA9-Pad68) -> Net-(U3-PA9)
- U3 pad 69: unconnected-(U3-PA10-Pad69) -> Net-(U3-PA10)
- U3 pad 70: unconnected-(U3-PA11-Pad70) -> /Charging_USB/USB_DM_MCU
- U3 pad 71: unconnected-(U3-PA12-Pad71) -> /Charging_USB/USB_DP_MCU
- U3 pad 72: unconnected-(U3-PA13-Pad72) -> Net-(U3-PA13)
- U3 pad 73: unconnected-(U3-VDDUSB-Pad73) -> /MCU/VUSB
- U3 pad 75: unconnected-(U3-VDD-Pad75) -> +3V3
- U3 pad 76: unconnected-(U3-PA14-Pad76) -> Net-(U3-PA14)
- U3 pad 78: unconnected-(U3-PC10-Pad78) -> Net-(U3-PC10)
- U3 pad 79: unconnected-(U3-PC11-Pad79) -> Net-(U3-PC11)
- U3 pad 80: unconnected-(U3-PC12-Pad80) -> Net-(U3-PC12)
- U3 pad 83: unconnected-(U3-PD2-Pad83) -> Net-(U3-PD2)
- U3 pad 95: unconnected-(U3-PB8-Pad95) -> Net-(U3-PB8)
- U3 pad 96: unconnected-(U3-PB9-Pad96) -> Net-(U3-PB9)
- U304 pad 14: +3V3 -> Net-(U304-VDD2)
- U304 pad 16: +3V3 -> Net-(U304-VBUS2)
- U305 pad 23: /Charging_USB/PLLFILT -> Net-(U305-PLLFILT)
- U4 pad 3: /Charging_USB/VSYS -> Net-(U4-EN)
- U4 pad 4: (no net) -> GND
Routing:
- net /Charging_Isolation/3V3: track 12.5 -> 0.00 mm
- net (no net): track 0.00 -> 12.5 mm
- net Net-(U1-DT1): track 0.00 -> 9.53 mm
- net Net-(U1-RFS1): track 0.00 -> 9.50 mm
- net /Charging_USB/DAB+: track 0.00 -> 9.45 mm
- net /Charging_Isolation/DA+: track 9.45 -> 0.00 mm
- net /Charging_USB/DAB-: track 0.00 -> 8.64 mm
- net /Charging_Isolation/DB-: track 8.64 -> 0.00 mm
- net /Charging_USB/VDD1: track 0.00 -> 8.54 mm
- net /Charging_Isolation/VDD1: track 8.54 -> 0.00 mm
- net Net-(U1-DR1): track 0.00 -> 5.30 mm
- net Net-(U1-SCLK1): track 0.00 -> 5.13 mm
- net /Charging_USB/UD-: track 0.00 -> 4.48 mm, vias 0 -> 1
- net /Charging_Isolation/UD-: track 4.48 -> 0.00 mm, vias 1 -> 0
- net /Charging_USB/UD+: track 0.00 -> 4.17 mm, vias 0 -> 1
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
